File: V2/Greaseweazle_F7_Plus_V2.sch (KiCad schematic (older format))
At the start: 77 parts, among them J1 Wurth 694106301002, J10 PIN1X2, J11 PIN1X2, J12 IDC Box Header, J2 USB_B, J3 Molex 105017-1001, J4 TE EI 171826-4, J5 PIN1X3, J6 PIN1X2, J7 PIN1X5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

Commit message: fixed footprint+silk of polarized caps
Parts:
- C21, C22, C23: footprint Capacitor_THT:C_Radial_D10.0mm_H20.0mm_P5.00mm -> Capacitor_THT:CP_Radial_D10.0mm_P5.00mm; symbol Device:C_Small -> Device:CP
- LOGO2: footprint greaseweazle:Greaseweazle_Logo_verysmall -> greaseweazle:Greaseweazle_Logo_small
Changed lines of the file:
@@
 	4400 3200 4400 3400
 $Comp
-L Device:C_Small C21
+L Device:CP C21
 U 1 1 61147C2B
 P 3700 10150
 F 0 "C21" H 3792 10196 50  0000 L CNN
 F 1 "1000uF" H 3792 10105 50  0000 L CNN
-F 2 "Capacitor_THT:C_Radial_D10.0mm_H20.0mm_P5.00mm" H 3700 10150 50  0001 C CNN
+F 2 "Capacitor_THT:CP_Radial_D10.0mm_P5.00mm" H 3700 10150 50  0001 C CNN
 F 3 "https://www.mouser.de/datasheet/2/977/e_PK-1601094.pdf" H 3700 10150 50  0001 C CNN
 F 4 "" H 3700 10150 50  0001 C CNN "LCSC"
@@
 $EndComp
 $Comp
-L Device:C_Small C22
+L Device:CP C22
 U 1 1 61147FE4
-P 4150 10150
-F 0 "C22" H 4242 10196 50  0000 L CNN
-F 1 "1000uF" H 4242 10105 50  0000 L CNN
-F 2 "Capacitor_THT:C_Radial_D10.0mm_H20.0mm_P5.00mm" H 4150 10150 50  0001 C CNN
-F 3 "https://www.mouser.de/datasheet/2/977/e_PK-1601094.pdf" H 4150 10150 50  0001 C CNN
-F 4 "" H 4150 10150 50  0001 C CNN "LCSC"
-F 5 "" H 4150 10150 50  0001 C CNN "MFR.Part"
-	1    4150 10150
+P 4200 10150
+F 0 "C22" H 4292 10196 50  0000 L CNN
+F 1 "1000uF" H 4292 10105 50  0000 L CNN
+F 2 "Capacitor_THT:CP_Radial_D10.0mm_P5.00mm" H 4200 10150 50  0001 C CNN
+F 3 "https://www.mouser.de/datasheet/2/977/e_PK-1601094.pdf" H 4200 10150 50  0001 C CNN
+F 4 "" H 4200 10150 50  0001 C CNN "LCSC"
+F 5 "" H 4200 10150 50  0001 C CNN "MFR.Part"
+	1    4200 10150
 	1    0    0    -1
 $EndComp
 $Comp
-L Device:C_Small C23
+L Device:CP C23
 U 1 1 6114903B
-P 4600 10150
-F 0 "C23" H 4692 10196 50  0000 L CNN
-F 1 "1000uF" H 4692 10105 50  0000 L CNN
-F 2 "Capacitor_THT:C_Radial_D10.0mm_H20.0mm_P5.00mm" H 4600 10150 50  0001 C CNN
-F 3 "https://www.mouser.de/datasheet/2/977/e_PK-1601094.pdf" H 4600 10150 50  0001 C CNN
-F 4 "" H 4600 10150 50  0001 C CNN "LCSC"
-F 5 "" H 4600 10150 50  0001 C CNN "MFR.Part"
-	1    4600 10150
+P 4700 10150
+F 0 "C23" H 4792 10196 50  0000 L CNN
+F 1 "1000uF" H 4792 10105 50  0000 L CNN
+F 2 "Capacitor_THT:CP_Radial_D10.0mm_P5.00mm" H 4700 10150 50  0001 C CNN
+F 3 "https://www.mouser.de/datasheet/2/977/e_PK-1601094.pdf" H 4700 10150 50  0001 C CNN
+F 4 "" H 4700 10150 50  0001 C CNN "LCSC"
+F 5 "" H 4700 10150 50  0001 C CNN "MFR.Part"
+	1    4700 10150
 	1    0    0    -1
 $EndComp
-Wire Wire Line
-	3100 9950 3700 9950
 Connection ~ 3100 9950
 Connection ~ 3100 10350
-Wire Wire Line
-	3700 10250 3700 10350
-Connection ~ 3700 10350
-Wire Wire Line
-	3700 10350 3100 10350
-Wire Wire Line
-	4150 10250 4150 10350
-Connection ~ 4150 10350
-Wire Wire Line
-	4150 10350 3700 10350
-Wire Wire Line
-	4600 10250 4600 10350
-Wire Wire Line
-	4600 10350 4150 10350
-Wire Wire Line
-	4600 10050 4600 9950
-Wire Wire Line
-	4150 10050 4150 9950
-Connection ~ 4150 9950
-Wire Wire Line
-	4150 9950 4600 9950
-Wire Wire Line
-	3700 10050 3700 9950
-Connection ~ 3700 9950
-Wire Wire Line
-	3700 9950 4150 9950
 $Comp
 L Graphic:Logo_Open_Hardware_Small LOGO2
@@
 F 0 "LOGO2" H 15400 10775 50  0001 C CNN
 F 1 "GW Logo" H 15400 10275 50  0001 C CNN
-F 2 "greaseweazle:Greaseweazle_Logo_verysmall" H 15400 10500 50  0001 C CNN
+F 2 "greaseweazle:Greaseweazle_Logo_small" H 15400 10500 50  0001 C CNN
 F 3 "~" H 15400 10500 50  0001 C CNN
 	1    15400 10500
 	1    0    0    -1
 $EndComp
+Wire Wire Line
+	3100 9950 3700 9950
+Wire Wire Line
+	3100 10350 3700 10350
+Wire Wire Line
+	3700 9950 3700 10000
+Connection ~ 3700 9950
+Wire Wire Line
+	3700 10300 3700 10350
+Connection ~ 3700 10350
+Wire Wire Line
+	3700 10350 4200 10350
+Wire Wire Line
+	4200 10300 4200 10350
+Connection ~ 4200 10350
+Wire Wire Line
+	4700 10300 4700 10350
+Wire Wire Line
+	4200 10350 4700 10350
+Wire Wire Line
+	4700 10000 4700 9950
+Wire Wire Line
+	3700 9950 4200 9950
+Wire Wire Line
+	4200 10000 4200 9950
+Connection ~ 4200 9950
+Wire Wire Line
+	4200 9950 4700 9950
 $EndSCHEMATC

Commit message: use enhanced floppy interface
use this document as reference: http://www.mcamafia.de/pdf/ps2_fdd_trm_s42g2194_00.pdf
IBM Personal System/2
3.5inch Diskette drives
Technical Reference 42G2194 S42G-2194-00

This version is no longer compatible to original firmware because
some connections changed

support additionally the following pins:
  media type ID 0+1
  drive type ID 0+1
  data rate selection 0+1
  disk change
  +5V (must be set using the "V5 Source" jumper J5)

removed connection from 7407 to pin6 (this is +12V)
pin 4 is now input instead of output
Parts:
- added R13, R14, R15, R16, R17: 1K0, Resistor_SMD:R_0805_2012Metric, symbol Device:R_Small
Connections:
- net +5V: now also J12.3 (Pin_3), R13.1, R14.1, R15.2, R16.2, R17.2
- net GND: no longer J12.17 (Pin_17), J12.27 (Pin_27), J12.3 (Pin_3), J12.33 (Pin_33), J12.9 (Pin_9)
- net ~MTYPE_ID0~: now reaches U4.20 (PA4)
- net ~MTYPE_ID0~: now also J12.27 (Pin_27), R17.1
- net ~MTYPE_ID1~: now reaches U4.21 (PA5)
- net ~MTYPE_ID1~: now also J12.17 (Pin_17), R16.1
- net ~DISK_CHANGE~: now reaches U4.41 (PA8)
- net ~DISK_CHANGE~: now also J12.34 (Pin_34), R13.2
- net ~DTYPE_ID0~: now reaches U4.44 (PA11)
- net ~DTYPE_ID0~: now also J12.9 (Pin_9), R15.1
- net ~DTYPE_ID1~: now reaches U4.45 (PA12)
- net ~DTYPE_ID1~: now also J12.4 (Pin_4), R14.2
- net ~PIN2_5V~ renamed ~DATA_RATE_SEL1_5V~
- net ~PIN2~ renamed ~DATA_RATE_SEL1~
- net ~PIN4_5V~ renamed ~DATA_RATE_SEL0_5V~
- net ~DATA_RATE_SEL0_5V~: now also J12.33 (Pin_33); no longer J12.4 (Pin_4)
- net ~PIN4~ renamed ~DATA_RATE_SEL0~
- net ~PIN6_5V~: no longer names the net of J12.6 (Pin_6)
- net ~PIN6_5V~: no longer U6.4
- net ~PIN6~: no longer names the net of U4.38 (PC7)
- net ~PIN6~: no longer U6.3
- no-connect marks 25 -> 24
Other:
- note added: "+12V n.c."
- note added: "PC7 Reserved, formerly\nused for pin6"
- note added: "Reserved, formerly used for\npin6 driven by PC7"
- note added: "TODO: check pin assignment:\nPin 3 is 5V\nPin 6 is +12V\ncheck also the “enhanced 34pin header interface”\nhttp://www.mcamafia.de/pdf/ps2_fdd_trm_s42g2194_00.pdf\n\n34-pin Header Interface, Media Sense\n This connector is for drives and controllers that support media sense.\nPin Signal Pin Signal\n 1 Ground 2 Data rate Select 1\n 3 + 5VDC 4 Drive Type ID1/Drive status 1\n 5 Ground 6 + 12VDC\n 7 G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"
- moved on the sheet: J11, J12, R5, R6, R7, R8

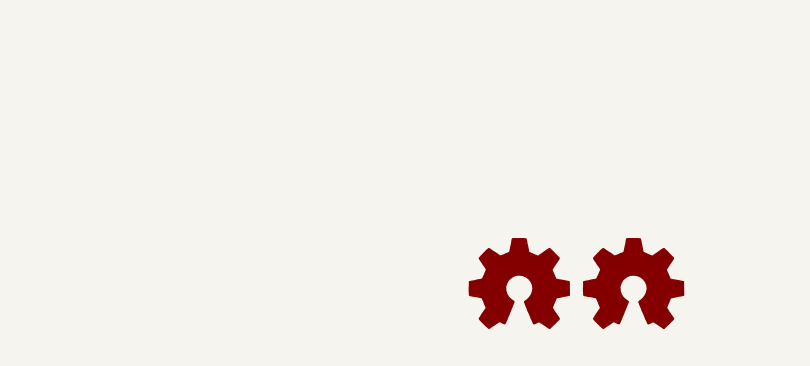
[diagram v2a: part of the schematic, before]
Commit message: moved components to optimize routing
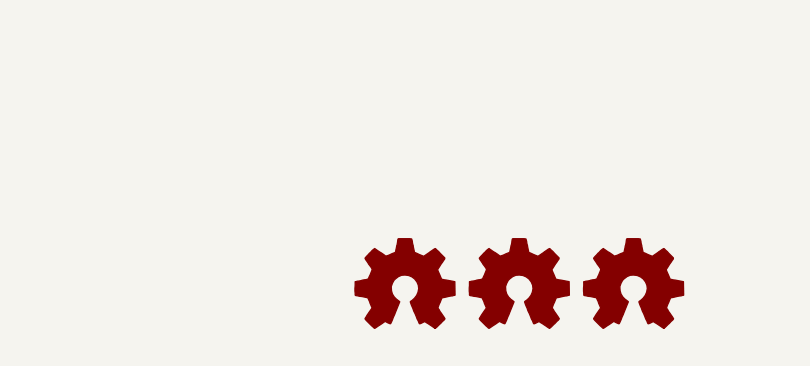
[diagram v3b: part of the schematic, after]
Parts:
- added LOGO3: GW Logo, Symbol:Symbol_Barrel_Polarity, symbol Graphic:Logo_Open_Hardware_Small
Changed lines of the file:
@@
 NoConn ~ 8550 5600
 NoConn ~ 1200 1100
+$Comp
+L Graphic:Logo_Open_Hardware_Small LOGO3
+U 1 1 612989CF
+P 14900 10500
+F 0 "LOGO3" H 14900 10775 50  0001 C CNN
+F 1 "GW Logo" H 14900 10275 50  0001 C CNN
+F 2 "Symbol:Symbol_Barrel_Polarity" H 14900 10500 50  0001 C CNN
+F 3 "~" H 14900 10500 50  0001 C CNN
+	1    14900 10500
+	1    0    0    -1
+$EndComp
 $EndSCHEMATC

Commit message: added user pin connector removed C23
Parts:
- removed C23: 1000uF, Capacitor_THT:CP_Radial_D10.0mm_P5.00mm, symbol Device:CP
- added J13: Conn_02x05_Odd_Even, Connector_PinHeader_2.54mm:PinHeader_2x08_P2.54mm_Vertical, symbol Connector_Generic:Conn_02x08_Odd_Even
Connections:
- net labels added: ~USER_PIN10~, ~USER_PIN11~, ~USER_PIN12~, ~USER_PIN1_OUT_5V~, ~USER_PIN1_OUT~, ~USER_PIN2~, ~USER_PIN3~, ~USER_PIN4~, ~USER_PIN5~, ~USER_PIN6~, ~USER_PIN7~, ~USER_PIN8~, ~USER_PIN9~
- wire segments 387 -> 413
- no-connect marks 24 -> 10
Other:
- note added: "User Pins"
- note removed: "PC7 Reserved, formerly\nused for pin6"
- note removed: "Reserved, formerly used for\npin6 driven by PC7"
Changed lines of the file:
@@
 Wire Wire Line
 	5700 8100 6500 8100
-NoConn ~ 5700 7700
-NoConn ~ 5700 7600
-NoConn ~ 5700 7500
-NoConn ~ 5700 7400
-NoConn ~ 5700 7300
-NoConn ~ 5700 7200
-NoConn ~ 4400 6800
-NoConn ~ 4400 8100
-NoConn ~ 4400 8000
-NoConn ~ 4400 7900
-NoConn ~ 5700 6700
-NoConn ~ 4400 7800
-NoConn ~ 4400 7500
 NoConn ~ 4400 7200
 NoConn ~ 4400 7100
 NoConn ~ 4400 7000
+NoConn ~ 5700 6700
+NoConn ~ 4400 7500
 NoConn ~ 4400 8400
 Text Label 6500 8000 2    50   ~ 0
@@
 Wire Wire Line
 	4400 7300 3600 7300
-$Comp
-L MCU_ST_STM32F7:STM32F732RETx U4
-U 1 1 5EAAE527
-P 5100 6800
-F 0 "U4" H 5100 6900 50  0000 C CNN
-F 1 "STM32F730R8T6" H 5100 6800 50  0000 C CNN
-F 2 "Package_QFP:LQFP-64_10x10mm_P0.5mm" H 4500 5100 50  0001 R CNN
-F 3 "https://datasheet.lcsc.com/szlcsc/2001031734_STMicroelectronics-STM32F730R8T6_C478453.pdf" H 5100 6800 50  0001 C CNN
-F 4 "C478453" H 5100 6800 50  0001 C CNN "LCSC"
-F 5 "STM32F730R8T6" H 5100 6800 50  0001 C CNN "MFR.Part"
-	1    5100 6800
-	1    0    0    -1
-$EndComp
 $Comp
 L Mechanical:MountingHole H1
@@
 Text Notes 12400 4700 0    50   ~ 10
 LEDs
-NoConn ~ 5700 7800
-Text Notes 3400 8050 0    50   ~ 0
+Text Notes 3350 8300 0    50   ~ 0
 PC15:13 used for ID2:0
 Text Label 11550 6850 0    50   ~ 0
@@
 	1    0    0    -1
 $EndComp
-$Comp
-L Device:CP C23
-U 1 1 6114903B
-P 4700 10150
-F 0 "C23" H 4792 10196 50  0000 L CNN
-F 1 "1000uF" H 4792 10105 50  0000 L CNN
-F 2 "Capacitor_THT:CP_Radial_D10.0mm_P5.00mm" H 4700 10150 50  0001 C CNN
-F 3 "https://www.mouser.de/datasheet/2/977/e_PK-1601094.pdf" H 4700 10150 50  0001 C CNN
-F 4 "" H 4700 10150 50  0001 C CNN "LCSC"
-F 5 "" H 4700 10150 50  0001 C CNN "MFR.Part"
-	1    4700 10150
-	1    0    0    -1
-$EndComp
 Connection ~ 3100 9950
 Connection ~ 3100 10350
@@
 Wire Wire Line
 	4200 10300 4200 10350
-Connection ~ 4200 10350
-Wire Wire Line
-	4700 10300 4700 10350
-Wire Wire Line
-	4200 10350 4700 10350
-Wire Wire Line
-	4700 10000 4700 9950
 Wire Wire Line
 	3700 9950 4200 9950
 Wire Wire Line
 	4200 10000 4200 9950
-Connection ~ 4200 9950
-Wire Wire Line
-	4200 9950 4700 9950
 Text Notes 14050 6500 0    50   ~ 0
 TODO: check pin assignment:\nPin 3 is 5V\nPin 6 is +12V\ncheck also the “enhanced 34pin header interface”\nhttp://www.mcamafia.de/pdf/ps2_fdd_trm_s42g2194_00.pdf\n\n34-pin Header Interface, Media Sense\n  This connector is for drives and controllers that support media sense.\nPin Signal                         Pin Signal\n 1 Ground                          2 Data rate Select 1\n 3 + 5VDC                          4 Drive Type ID1/Drive status 1\n 5 Ground                          6 + 12VDC\n 7 Ground                          8 -Index\n 9 Drive Type ID0/Drive status 0  10 Reserved\n11 Ground                         12 -Drive Select\n13 Ground                         14 -Security Command*\n15 Ground                         16 -Motor Enable\n17 Media Type ID1/Drive status 3  18 -Direction In\n19 Ground                         20 -Step\n21 Ground                         22 -Write Data\n23 Ground                         24 -Write Enable\n25 Ground                         26 -Track 0\n27 Media Type ID0/Drive status 2  28 -Write Protect\n29 Ground                         30 -Read Data\n31 Ground                         32 -Head 1 Select\n33 Data rate Select 0             34 -Diskette Change\nFigure 10.  Signal Assignments For the Enhanced 34-pin Header Interface\n* '90 ref has this Reserved\nAll blue text is not present in '90 Tech Ref
@@
 Text Notes 12550 7000 0    50   ~ 0
 +12V n.c.
-Text Notes 9650 5650 0    50   ~ 0
-Reserved, formerly used for\npin6 driven by PC7
-Text Notes 3450 7600 0    50   ~ 0
-PC7 Reserved, formerly\nused for pin6
-NoConn ~ 4400 7600
-NoConn ~ 9150 5600
-NoConn ~ 8550 5600
 NoConn ~ 1200 1100
 $Comp
@@
 	1    0    0    -1
 $EndComp
+Wire Wire Line
+	8550 5600 7750 5600
+Text Label 7750 5600 0    50   ~ 0
+~USER_PIN1_OUT~
+Wire Wire Line
+	9150 5600 10350 5600
+Text Label 9650 5600 0    50   ~ 0
+~USER_PIN1_OUT_5V~
+Wire Wire Line
+	4400 7600 3600 7600
+Text Label 3600 7600 0    50   ~ 0
+~USER_PIN1_OUT~
+$Comp
+L MCU_ST_STM32F7:STM32F732RETx U4
+U 1 1 5EAAE527
+P 5100 6800
+F 0 "U4" H 5100 6900 50  0000 C CNN
+F 1 "STM32F730R8T6" H 5100 6800 50  0000 C CNN
+F 2 "Package_QFP:LQFP-64_10x10mm_P0.5mm" H 4500 5100 50  0001 R CNN
+F 3 "https://datasheet.lcsc.com/szlcsc/2001031734_STMicroelectronics-STM32F730R8T6_C478453.pdf" H 5100 6800 50  0001 C CNN
+F 4 "C478453" H 5100 6800 50  0001 C CNN "LCSC"
+F 5 "STM32F730R8T6" H 5100 6800 50  0001 C CNN "MFR.Part"
+	1    5100 6800
+	1    0    0    -1
+$EndComp
+Wire Wire Line
+	5700 7200 6500 7200
+Wire Wire Line
+	5700 7300 6500 7300
+Wire Wire Line
+	5700 7400 6500 7400
+Wire Wire Line
+	5700 7500 6500 7500
+Wire Wire Line
+	5700 7600 6500 7600
+Wire Wire Line
+	5700 7700 6500 7700
+Wire Wire Line
+	5700 7800 6500 7800
+Text Label 6100 7200 0    50   ~ 0
+~USER_PIN2~
+Text Label 6100 7300 0    50   ~ 0
+~USER_PIN3~
+Text Label 6100 7400 0    50   ~ 0
+~USER_PIN4~
+Text Label 6100 7500 0    50   ~ 0
+~USER_PIN5~
+Text Label 6100 7600 0    50   ~ 0
+~USER_PIN6~
+Text Label 6100 7700 0    50   ~ 0
+~USER_PIN7~
+Text Label 6100 7800 0    50   ~ 0
+~USER_PIN8~
+$Comp
+L Connector_Generic:Conn_02x08_Odd_Even J13
+U 1 1 616411D7
+P 8650 8800
+F 0 "J13" H 8700 9317 50  0000 C CNN
+F 1 "Conn_02x05_Odd_Even" H 8700 9226 50  0000 C CNN
+F 2 "Connector_PinHeader_2.54mm:PinHeader_2x08_P2.54mm_Vertical" H 8650 8800 50  0001 C CNN
+F 3 "~" H 8650 8800 50  0001 C CNN
+	1    8650 8800
+	1    0    0    -1
+$EndComp
+Wire Wire Line
+	8450 8500 7700 8500
+Wire Wire Line
+	8450 8600 7650 8600
+Wire Wire Line
+	8450 8700 7650 8700
+Wire Wire Line
+	8450 8800 7650 8800
+Wire Wire Line
+	8450 8900 7650 8900
+Wire Wire Line
+	9700 8500 8950 8500
+Wire Wire Line
+	9750 8600 8950 8600
+Wire Wire Line
+	9750 8700 8950 8700
+Wire Wire Line
+	9750 8800 8950 8800
+Wire Wire Line
+	9750 8900 8950 8900
+$Comp
+L power:GND #PWR0110
+U 1 1 618199B0
+P 7700 8500
+F 0 "#PWR0110" H 7700 8250 50  0001 C CNN
+F 1 "GND" V 7700 8300 50  0000 C CNN
+F 2 "" H 7700 8500 50  0001 C CNN
+F 3 "" H 7700 8500 50  0001 C CNN
+	1    7700 8500
+	0    1    1    0
+$EndComp
+$Comp
+L power:+3V3 #PWR0111
+U 1 1 61819FC1
+P 9700 8500
+F 0 "#PWR0111" H 9700 8350 50  0001 C CNN
+F 1 "+3V3" H 9715 8673 50  0000 C CNN
+F 2 "" H 9700 8500 50  0001 C CNN
+F 3 "" H 9700 8500 50  0001 C CNN
+	1    9700 8500
+	0    1    1    0
+$EndComp
+Text Label 7650 8600 0    50   ~ 0
+~USER_PIN1_OUT_5V~
+Text Label 7650 8700 0    50   ~ 0
+~USER_PIN3~
+Text Label 9350 8600 0    50   ~ 0
+~USER_PIN2~
+Text Label 9350 8700 0    50   ~ 0
+~USER_PIN4~
+Text Label 9350 8800 0    50   ~ 0
+~USER_PIN6~
+Text Label 9350 8900 0    50   ~ 0
+~USER_PIN8~
+Text Label 7650 8800 0    50   ~ 0
+~USER_PIN5~
+Text Label 7650 8900 0    50   ~ 0
+~USER_PIN7~
+Text Notes 8500 8200 0    50   ~ 10
+User Pins
+Wire Wire Line
+	3600 6800 4400 6800
+Text Label 3600 6800 0    50   ~ 0
+~USER_PIN9~
+Wire Wire Line
+	3600 7900 4400 7900
+Text Label 3600 7900 0    50   ~ 0
+~USER_PIN10~
+Wire Wire Line
+	3600 8000 4400 8000
+Text Label 3600 8000 0    50   ~ 0
+~USER_PIN11~
+Wire Wire Line
+	3600 8100 4400 8100
+Text Label 3600 8100 0    50   ~ 0
+~USER_PIN12~
+NoConn ~ 4400 7800
+Wire Wire Line
+	9750 9000 8950 9000
+Text Label 9300 9000 0    50   ~ 0
+~USER_PIN10~
+Wire Wire Line
+	9750 9100 8950 9100
+Text Label 9300 9100 0    50   ~ 0
+~USER_PIN12~
+Wire Wire Line
+	8450 9000 7650 9000
+Text Label 7650 9000 0    50   ~ 0
+~USER_PIN9~
+Wire Wire Line
+	8450 9100 7650 9100
+Text Label 7650 9100 0    50   ~ 0
+~USER_PIN11~
+Wire Wire Line
+	8950 9200 9750 9200
+$Comp
+L power:+5V #PWR?
+U 1 1 61F37FE7
+P 9750 9200
+F 0 "#PWR?" H 9750 9050 50  0001 C CNN
+F 1 "+5V" V 9750 9350 50  0000 L CNN
+F 2 "" H 9750 9200 50  0001 C CNN
+F 3 "" H 9750 9200 50  0001 C CNN
+	1    9750 9200
+	0    1    1    0
+$EndComp
+Wire Wire Line
+	7650 9200 8450 9200
+Text Label 7650 9200 0    50   ~ 0
+USB_VBUS
 $EndSCHEMATC
